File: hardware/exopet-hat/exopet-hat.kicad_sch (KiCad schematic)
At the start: 67 parts, among them J1 12V DC in, J10 CH3 12V OUT, J11 CH4 dry contact, J13 FLOAT1 switch, J14 FLOAT2 switch, J3 RPi GPIO (HAT), J4 TEMP (3V3/DATA/GND), J8 CH1 12V OUT, J9 CH2 12V OUT, K1 G5LE-1-CF DC12, K2 G5LE-1-CF DC12, K3 G5LE-1-CF DC12, K4 G5LE-1-CF DC12, Q1 AOD403, U2 TBD62003AFG, U4 CAT24C32, U5 5V ESD clamp (SOD-323), U6 TPS54302DDC

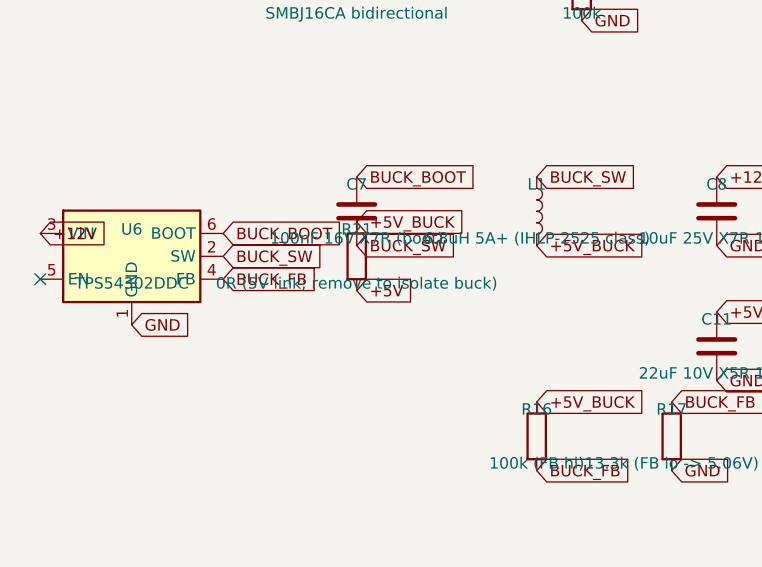
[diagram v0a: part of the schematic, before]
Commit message: HAT rev 2 + enclosure: DS18B20 R/Y/B wire markings; R21 current-rating fix; hard-fail preflight
'Are you sure' audit of my own R21 change found three real issues:
C17477 was an unverified from-memory LCSC code; an 0805 zero-ohm
jumper (~2A) under-rates the Pi 4's 3A-peak 5V rail; and preflight's
piped exit codes meant gates could not actually fail the run. R21 is
now a 1206 with a rated>=3A matching hint, relocated collision-free,
and preflight hard-fails on any gate via explicit pass-token checks.

TEMP terminal gets R/Y/B markings (DS18B20 red=3V3, yellow=data,
black=GND) on both the board silk and the enclosure lid beside the
screw slot. All gates green.

Co-Authored-By: Claude Fable 5 <noreply@anthropic.com>
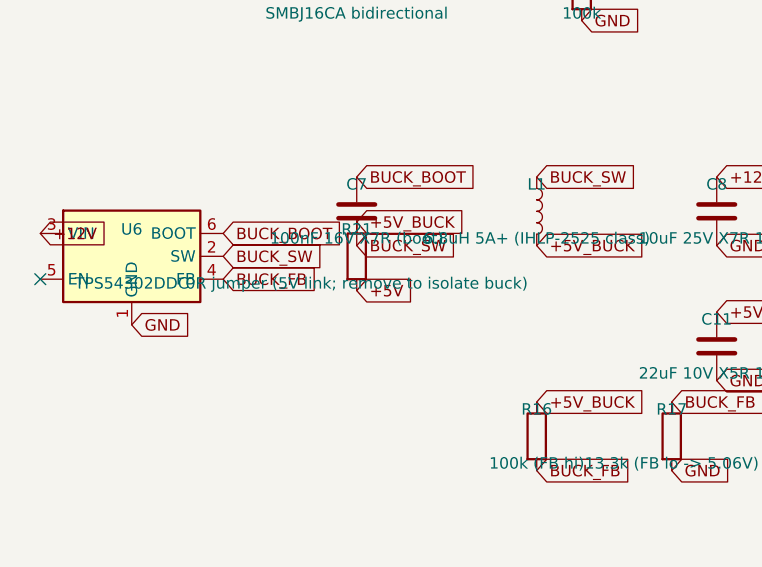
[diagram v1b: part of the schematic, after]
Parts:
- R21: value 0R (5V link; remove to isolate buck) -> 0R jumper (5V link; remove to isolate buck); footprint Resistor_SMD:R_0805_2012Metric -> Resistor_SMD:R_1206_3216Metric; LCSC C17477 -> VERIFY
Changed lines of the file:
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@@
     (exclude_from_sim no) (in_bom yes) (on_board yes) (dnp no)
     (property "Reference" "R21" (at 55 87 0) (effects (font (size 1.27 1.27))))
-    (property "Value" "0R (5V link; remove to isolate buck)" (at 55 93 0) (effects (font (size 1.27 1.27))))
-    (property "Footprint" "Resistor_SMD:R_0805_2012Metric" (at 55 90 0) (effects (font (size 1.27 1.27)) hide))
-    (property "LCSC" "C17477" (at 55 90 0) (effects (font (size 1.27 1.27)) hide))
+    (property "Value" "0R jumper (5V link; remove to isolate buck)" (at 55 93 0) (effects (font (size 1.27 1.27))))
+    (property "Footprint" "Resistor_SMD:R_1206_3216Metric" (at 55 90 0) (effects (font (size 1.27 1.27)) hide))
+    (property "LCSC" "VERIFY" (at 55 90 0) (effects (font (size 1.27 1.27)) hide))
     (pin "1")
     (pin "2")

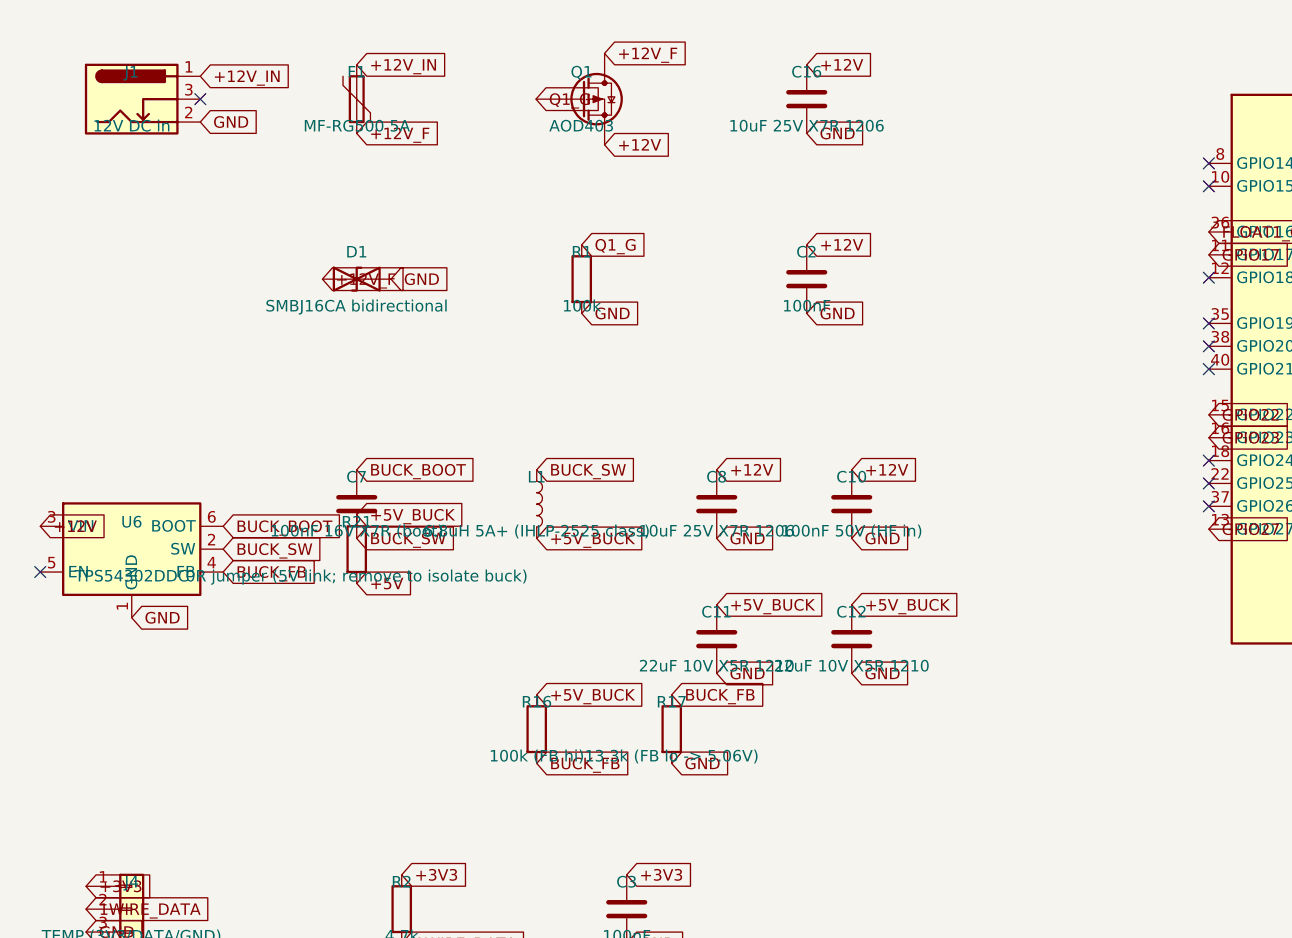
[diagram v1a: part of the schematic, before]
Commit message: HAT rev 2: apply all 7 fresh-eyes review fixes
- D3 B550C safety diode replaces R21 (HAT-guide compliant back-power;
  kills the USB-C->barrel-jack back-feed; no 2A jumper in the 5V path);
  buck setpoint raised to 5.40V pre-diode (R17 13.3k->12.4k)
- C17 75pF feedforward across R16 (TI Table 7-2, all-ceramic Cout)
- C1 100uF 25V low-profile SMD electrolytic restores input bulk
- F1 MF-RG500 -> MF-RG700 (hold current derating vs ~4.6A full load)
- D1 TVS moved from 40mm away to the input corner it protects
- ORDERING.md/BRINGUP.md rewritten for the new power architecture
- float conditioning resistors relocated near their terminals

New gate: check_drc_sanity.py re-measures every claimed clearance pair
from board geometry — kicad-cli emits phantom violations citing items
20.6mm apart as 0.055mm; phantoms are excused only with printed
measured proof. Preflight fully green: 69 parts, 212-pin golden audit,
DRC 0 real / 0 unconnected.

Co-Authored-By: Claude Fable 5 <noreply@anthropic.com>
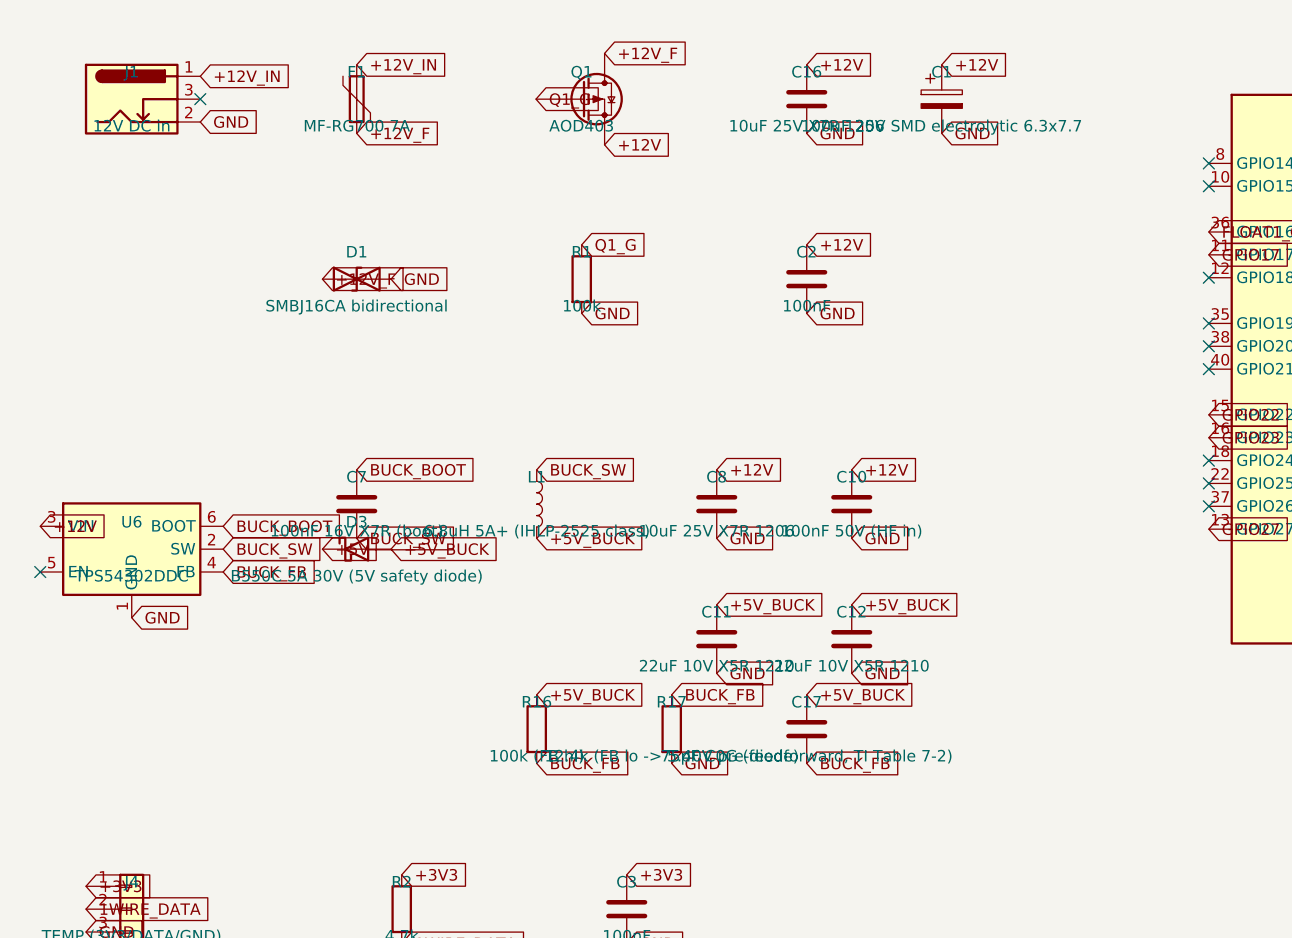
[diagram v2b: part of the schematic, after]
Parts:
- removed R21: 0R jumper (5V link; remove to isolate buck), Resistor_SMD:R_1206_3216Metric, symbol Device:R
- added C1: 100uF 25V SMD electrolytic 6.3x7.7, Capacitor_SMD:CP_Elec_6.3x7.7, symbol Device:C_Polarized
- added C17: 75pF C0G (feedforward, TI Table 7-2), Capacitor_SMD:C_0805_2012Metric, symbol Device:C
- added D3: B550C 5A 30V (5V safety diode), Diode_SMD:D_SMB, symbol Device:D_Schottky
- F1: value MF-RG500 5A -> MF-RG700 7A
- R17: value 13.3k (FB lo -> 5.06V) -> 12.4k (FB lo -> 5.40V pre-diode)
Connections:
- net +12V: now also C1.1
- net +5V: now also D3.1 (K)
- net +5V_BUCK: now also C17.1, D3.2 (A)
- net BUCK_FB: now also C17.2
- net GND: now also C1.2
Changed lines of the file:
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@@
     (exclude_from_sim no) (in_bom yes) (on_board yes) (dnp no)
     (property "Reference" "F1" (at 55 37 0) (effects (font (size 1.27 1.27))))
-    (property "Value" "MF-RG500 5A" (at 55 43 0) (effects (font (size 1.27 1.27))))
+    (property "Value" "MF-RG700 7A" (at 55 43 0) (effects (font (size 1.27 1.27))))
     (property "Footprint" "Fuse:Fuse_Bourns_MF-RG500" (at 55 40 0) (effects (font (size 1.27 1.27)) hide))
     (property "LCSC" "VERIFY" (at 55 40 0) (effects (font (size 1.27 1.27)) hide))
@@
     )
   )
+  (symbol (lib_id "Device:C_Polarized") (at 120 40 0) (unit 1)
+    (exclude_from_sim no) (in_bom yes) (on_board yes) (dnp no)
+    (property "Reference" "C1" (at 120 37 0) (effects (font (size 1.27 1.27))))
+    (property "Value" "100uF 25V SMD electrolytic 6.3x7.7" (at 120 43 0) (effects (font (size 1.27 1.27))))
+    (property "Footprint" "Capacitor_SMD:CP_Elec_6.3x7.7" (at 120 40 0) (effects (font (size 1.27 1.27)) hide))
+    (property "LCSC" "VERIFY" (at 120 40 0) (effects (font (size 1.27 1.27)) hide))
+    (pin "1")
+    (pin "2")
+    (instances
+      (project "exopet-hat"
+        (path "/e0a7e100-0000-4000-8000-00000000c0de" (reference "C1") (unit 1))
+      )
+    )
+  )
   (symbol (lib_id "Device:C") (at 105 60 0) (unit 1)
     (exclude_from_sim no) (in_bom yes) (on_board yes) (dnp no)
@@
     (exclude_from_sim no) (in_bom yes) (on_board yes) (dnp no)
     (property "Reference" "R17" (at 90 107 0) (effects (font (size 1.27 1.27))))
-    (property "Value" "13.3k (FB lo -> 5.06V)" (at 90 113 0) (effects (font (size 1.27 1.27))))
+    (property "Value" "12.4k (FB lo -> 5.40V pre-diode)" (at 90 113 0) (effects (font (size 1.27 1.27))))
     (property "Footprint" "Resistor_SMD:R_0805_2012Metric" (at 90 110 0) (effects (font (size 1.27 1.27)) hide))
     (property "LCSC" "VERIFY" (at 90 110 0) (effects (font (size 1.27 1.27)) hide))
@@
       (project "exopet-hat"
         (path "/e0a7e100-0000-4000-8000-00000000c0de" (reference "R17") (unit 1))
+      )
+    )
+  )
+  (symbol (lib_id "Device:C") (at 105 110 0) (unit 1)
+    (exclude_from_sim no) (in_bom yes) (on_board yes) (dnp no)
+    (property "Reference" "C17" (at 105 107 0) (effects (font (size 1.27 1.27))))
+    (property "Value" "75pF C0G (feedforward, TI Table 7-2)" (at 105 113 0) (effects (font (size 1.27 1.27))))
+    (property "Footprint" "Capacitor_SMD:C_0805_2012Metric" (at 105 110 0) (effects (font (size 1.27 1.27)) hide))
+    (property "LCSC" "VERIFY" (at 105 110 0) (effects (font (size 1.27 1.27)) hide))
+    (pin "1")
+    (pin "2")
+    (instances
+      (project "exopet-hat"
+        (path "/e0a7e100-0000-4000-8000-00000000c0de" (reference "C17") (unit 1))
       )
     )
@@
     )
   )
-  (symbol (lib_id "Device:R") (at 55 90 0) (unit 1)
-    (exclude_from_sim no) (in_bom yes) (on_board yes) (dnp no)
-    (property "Reference" "R21" (at 55 87 0) (effects (font (size 1.27 1.27))))
-    (property "Value" "0R jumper (5V link; remove to isolate buck)" (at 55 93 0) (effects (font (size 1.27 1.27))))
-    (property "Footprint" "Resistor_SMD:R_1206_3216Metric" (at 55 90 0) (effects (font (size 1.27 1.27)) hide))
+  (symbol (lib_id "Device:D_Schottky") (at 55 90 0) (unit 1)
+    (exclude_from_sim no) (in_bom yes) (on_board yes) (dnp no)
+    (property "Reference" "D3" (at 55 87 0) (effects (font (size 1.27 1.27))))
+    (property "Value" "B550C 5A 30V (5V safety diode)" (at 55 93 0) (effects (font (size 1.27 1.27))))
+    (property "Footprint" "Diode_SMD:D_SMB" (at 55 90 0) (effects (font (size 1.27 1.27)) hide))
     (property "LCSC" "VERIFY" (at 55 90 0) (effects (font (size 1.27 1.27)) hide))
     (pin "1")
@@
     (instances
       (project "exopet-hat"
-        (path "/e0a7e100-0000-4000-8000-00000000c0de" (reference "R21") (unit 1))
+        (path "/e0a7e100-0000-4000-8000-00000000c0de" (reference "D3") (unit 1))
       )
     )
@@
   (global_label "+12V" (shape input) (at 105.0 36.19 0) (effects (font (size 1.27 1.27)) (justify left)))
   (global_label "GND" (shape input) (at 105.0 43.81 0) (effects (font (size 1.27 1.27)) (justify left)))
+  (global_label "+12V" (shape input) (at 120.0 36.19 0) (effects (font (size 1.27 1.27)) (justify left)))
+  (global_label "GND" (shape input) (at 120.0 43.81 0) (effects (font (size 1.27 1.27)) (justify left)))
   (global_label "+12V" (shape input) (at 105.0 56.19 0) (effects (font (size 1.27 1.27)) (justify left)))
   (global_label "GND" (shape input) (at 105.0 63.81 0) (effects (font (size 1.27 1.27)) (justify left)))
@@
   (global_label "BUCK_FB" (shape input) (at 90.0 106.19 0) (effects (font (size 1.27 1.27)) (justify left)))
   (global_label "GND" (shape input) (at 90.0 113.81 0) (effects (font (size 1.27 1.27)) (justify left)))
+  (global_label "+5V_BUCK" (shape input) (at 105.0 106.19 0) (effects (font (size 1.27 1.27)) (justify left)))
+  (global_label "BUCK_FB" (shape input) (at 105.0 113.81 0) (effects (font (size 1.27 1.27)) (justify left)))
   (global_label "+12V" (shape input) (at 30.0 236.19 0) (effects (font (size 1.27 1.27)) (justify left)))
   (global_label "LED12V_A" (shape input) (at 30.0 243.81 0) (effects (font (size 1.27 1.27)) (justify left)))
@@
   (global_label "+3V3" (shape input) (at 125.0 240.0 0) (effects (font (size 1.27 1.27)) (justify left)))
   (global_label "GND" (shape input) (at 140.0 240.0 0) (effects (font (size 1.27 1.27)) (justify left)))
-  (global_label "+5V_BUCK" (shape input) (at 55.0 86.19 0) (effects (font (size 1.27 1.27)) (justify left)))
-  (global_label "+5V" (shape input) (at 55.0 93.81 0) (effects (font (size 1.27 1.27)) (justify left)))
+  (global_label "+5V" (shape input) (at 51.19 90.0 0) (effects (font (size 1.27 1.27)) (justify left)))
+  (global_label "+5V_BUCK" (shape input) (at 58.81 90.0 0) (effects (font (size 1.27 1.27)) (justify left)))
   (global_label "+3V3" (shape input) (at 175.08 36.98 0) (effects (font (size 1.27 1.27)) (justify left)))
   (global_label "+3V3" (shape input) (at 175.08 36.98 0) (effects (font (size 1.27 1.27)) (justify left)))

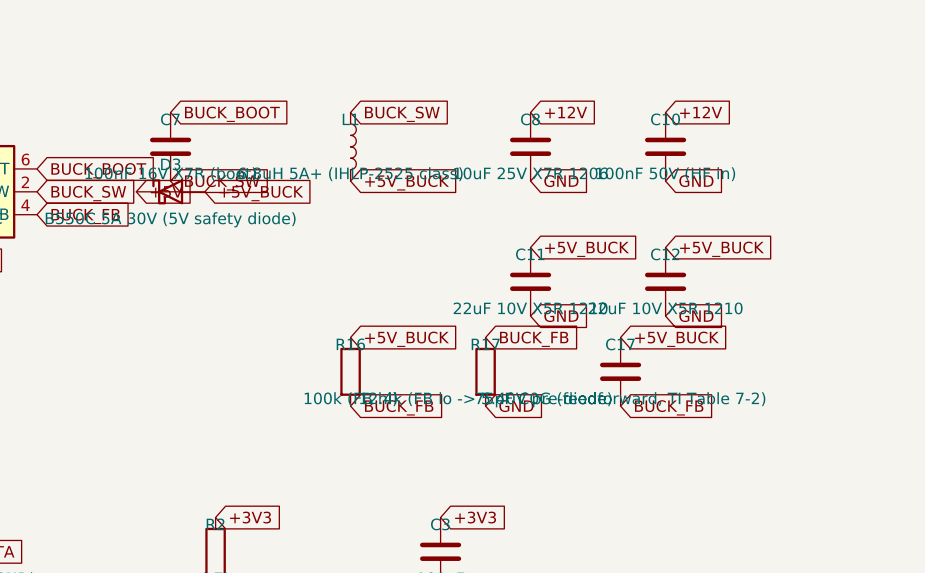
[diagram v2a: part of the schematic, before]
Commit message: HAT rev 2: round-2 review fixes — buck corners + F1 BOM pin
10uH inductor (HS current-limit margin at tolerance corners), 25V X7R
output caps (DC-bias derating), 12.7k FB (5.29V — Pi stays under +5%
at light load), F1 BOM unpinned (was still the 5A part code after the
7A value change — panel caught the incomplete fix). GPIO23 gets a
locked pre-route (down the J3 column midline, via, U2 escape) after
repeated seed strandings; float debounce caps C5/C6 move beside their
terminals. DRC sanity filter generalized to all geometric violation
types (phantoms now include shorting/mask reports citing items 3-20mm
apart). Preflight fully green; review package rebuilt with round-2
findings + honest lens coverage map for the human reviewer.

Co-Authored-By: Claude Fable 5 <noreply@anthropic.com>
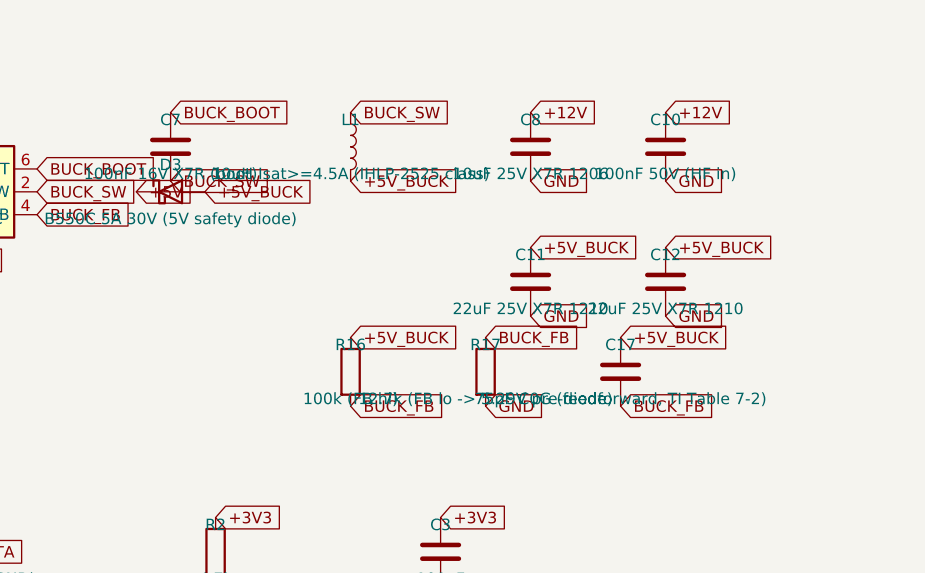
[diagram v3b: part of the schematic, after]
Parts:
- C11, C12: value 22uF 10V X5R 1210 -> 22uF 25V X7R 1210
- L1: value 6.8uH 5A+ (IHLP-2525 class) -> 10uH Isat>=4.5A (IHLP-2525 class)
- R17: value 12.4k (FB lo -> 5.40V pre-diode) -> 12.7k (FB lo -> 5.29V pre-diode)
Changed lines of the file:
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@@
     (exclude_from_sim no) (in_bom yes) (on_board yes) (dnp no)
     (property "Reference" "L1" (at 75 82 0) (effects (font (size 1.27 1.27))))
-    (property "Value" "6.8uH 5A+ (IHLP-2525 class)" (at 75 88 0) (effects (font (size 1.27 1.27))))
+    (property "Value" "10uH Isat>=4.5A (IHLP-2525 class)" (at 75 88 0) (effects (font (size 1.27 1.27))))
     (property "Footprint" "Inductor_SMD:L_Vishay_IHLP-2525" (at 75 85 0) (effects (font (size 1.27 1.27)) hide))
     (property "LCSC" "VERIFY" (at 75 85 0) (effects (font (size 1.27 1.27)) hide))
@@
     (exclude_from_sim no) (in_bom yes) (on_board yes) (dnp no)
     (property "Reference" "C11" (at 95 97 0) (effects (font (size 1.27 1.27))))
-    (property "Value" "22uF 10V X5R 1210" (at 95 103 0) (effects (font (size 1.27 1.27))))
+    (property "Value" "22uF 25V X7R 1210" (at 95 103 0) (effects (font (size 1.27 1.27))))
     (property "Footprint" "Capacitor_SMD:C_1210_3225Metric" (at 95 100 0) (effects (font (size 1.27 1.27)) hide))
     (property "LCSC" "VERIFY" (at 95 100 0) (effects (font (size 1.27 1.27)) hide))
@@
     (exclude_from_sim no) (in_bom yes) (on_board yes) (dnp no)
     (property "Reference" "C12" (at 110 97 0) (effects (font (size 1.27 1.27))))
-    (property "Value" "22uF 10V X5R 1210" (at 110 103 0) (effects (font (size 1.27 1.27))))
+    (property "Value" "22uF 25V X7R 1210" (at 110 103 0) (effects (font (size 1.27 1.27))))
     (property "Footprint" "Capacitor_SMD:C_1210_3225Metric" (at 110 100 0) (effects (font (size 1.27 1.27)) hide))
     (property "LCSC" "VERIFY" (at 110 100 0) (effects (font (size 1.27 1.27)) hide))
@@
     (exclude_from_sim no) (in_bom yes) (on_board yes) (dnp no)
     (property "Reference" "R17" (at 90 107 0) (effects (font (size 1.27 1.27))))
-    (property "Value" "12.4k (FB lo -> 5.40V pre-diode)" (at 90 113 0) (effects (font (size 1.27 1.27))))
+    (property "Value" "12.7k (FB lo -> 5.29V pre-diode)" (at 90 113 0) (effects (font (size 1.27 1.27))))
     (property "Footprint" "Resistor_SMD:R_0805_2012Metric" (at 90 110 0) (effects (font (size 1.27 1.27)) hide))
     (property "LCSC" "VERIFY" (at 90 110 0) (effects (font (size 1.27 1.27)) hide))
